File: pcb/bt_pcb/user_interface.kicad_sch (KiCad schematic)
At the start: 69 parts, among them J10 AudioJack3_Switch, J11 AudioJack3_Switch, J16 AudioJack3_Switch, J4 Conn_01x10, J9 AudioJack3_Switch, SW1 SW_Push, SW10 RotaryEncoder_Switch, SW2 SW_Push, SW3 SW_Push, SW4 SW_Push, SW5 SW_Push, SW6 SW_Push, SW7 SW_Push, SW8 SW_Push, SW9 SW_Push

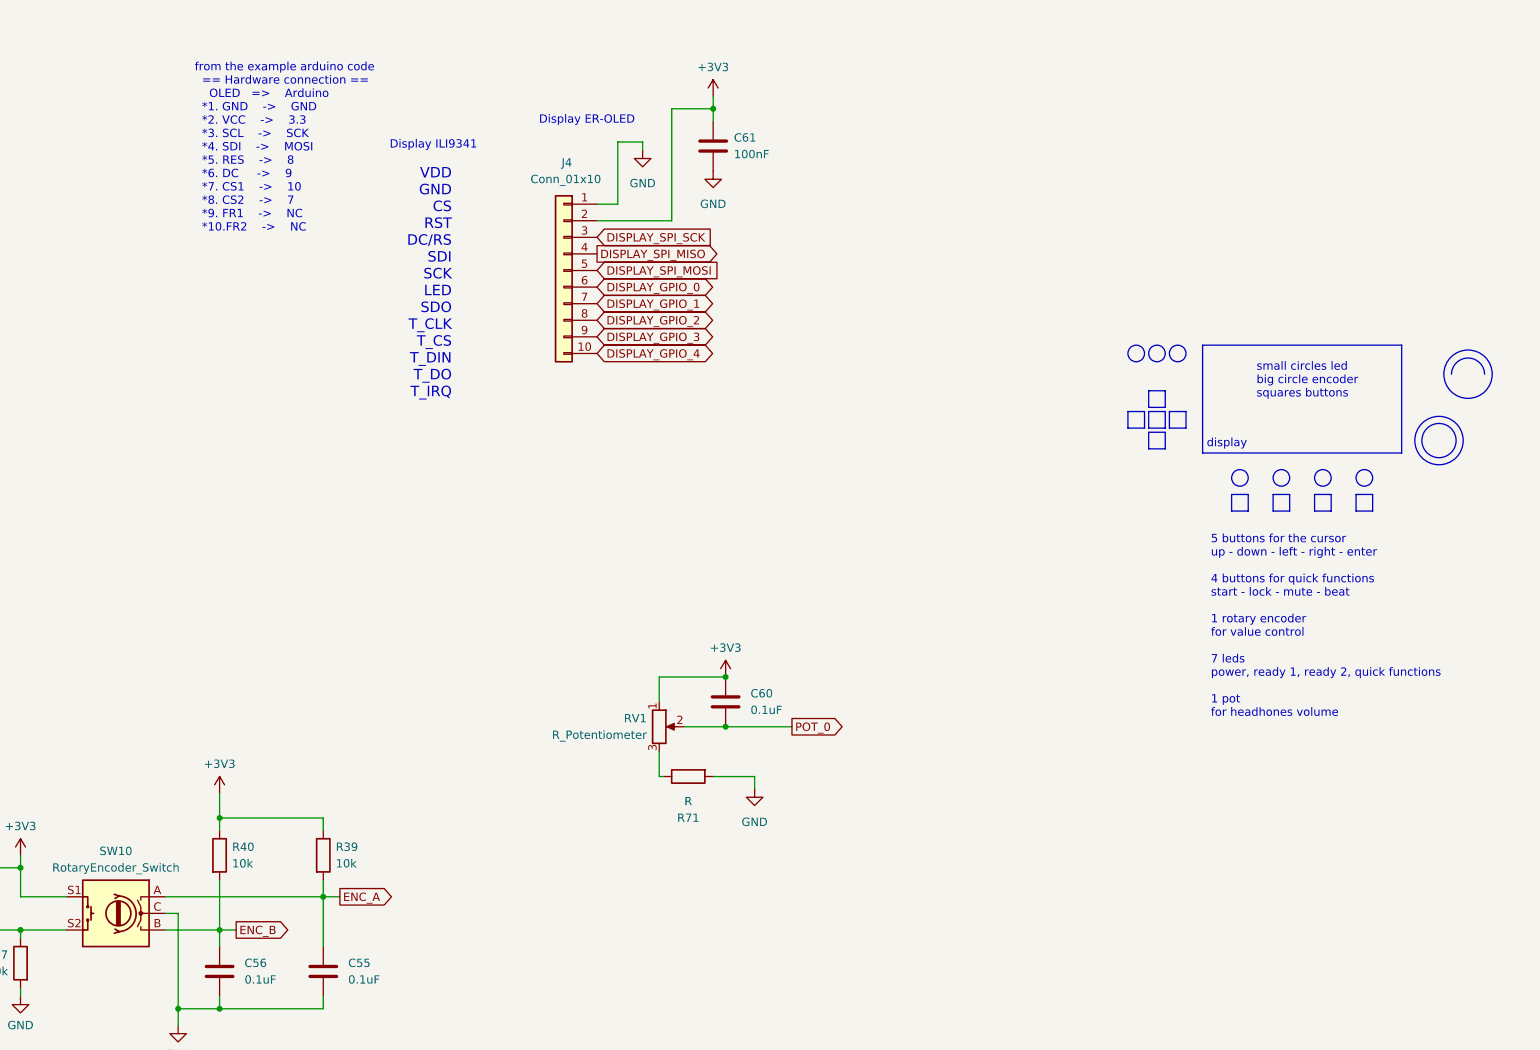
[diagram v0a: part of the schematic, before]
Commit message: ditching power pcb, new codec
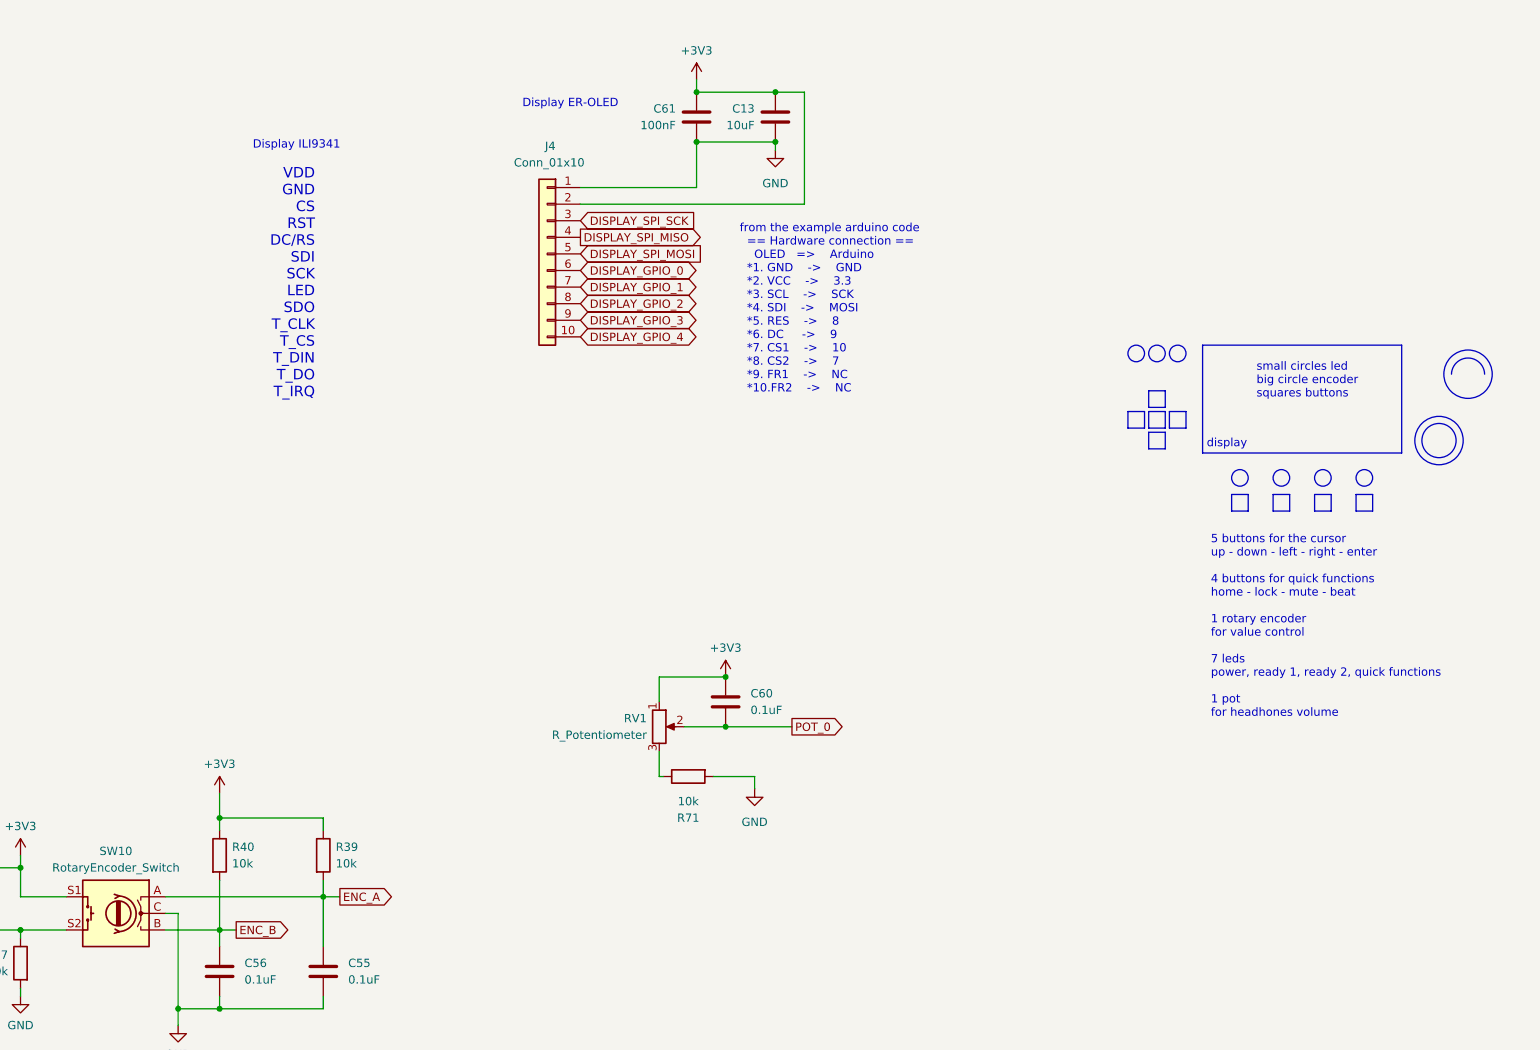
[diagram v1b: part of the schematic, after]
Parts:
- added C13: 10uF, symbol Device:C
- R71: value R -> 10k
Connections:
- net +3V3: now also C13.2
- net GND: now also C13.1
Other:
- note added: "5 buttons for the cursor up - down - left - right - enter 4 buttons for quick functions home - lock - mute - beat 1 rotary encoder for value control 7 leds power, ready 1, ready 2, quick functions 1 pot for headhones volume"
- note removed: "5 buttons for the cursor up - down - left - right - enter 4 buttons for quick functions start - lock - mute - beat 1 rotary encoder for value control 7 leds power, ready 1, ready 2, quick functions 1 pot for headhones volume"
- moved on the sheet: C61, J4

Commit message: big progress, now revising error and warnings
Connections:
- net BTN_0 renamed BTN_0_J
- net BTN_1 renamed BTN_1_J
- net BTN_2 renamed BTN_2_J
- net BTN_3 renamed BTN_3_J
- net BTN_4 renamed BTN_4_J
- net BTN_5 renamed BTN_5_QB
- net BTN_6 renamed BTN_6_QB
- net BTN_7 renamed BTN_7_QB
- net BTN_8 renamed BTN_8_QB
- net LED_0 renamed LED_0_RD
- net LED_1 renamed LED_1_RD
- net LED_2 renamed LED_2_QB
- net LED_3 renamed LED_3_QB
- net LED_4 renamed LED_4_QB
- net LED_5 renamed LED_5_QB
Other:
- note added: "2 leds are "mcu ready" so one for h750 and one for h523"
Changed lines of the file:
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@@
+		)
+	)
+	(text "2 leds are \"mcu ready\"\nso one for h750 and one for h523"
+		(exclude_from_sim no)
+		(at 332.74 138.43 0)
+		(effects
+			(font
+				(size 1.27 1.27)
+			)
 		)
 	)
@@
 	(wire
 		(pts
-			(xy 349.25 190.5) (xy 347.345 190.5)
+			(xy 347.98 190.5) (xy 347.345 190.5)
 		)
 		(stroke
@@
 	(wire
 		(pts
-			(xy 323.85 190.5) (xy 321.945 190.5)
+			(xy 322.58 190.5) (xy 321.945 190.5)
 		)
 		(stroke
@@
 	(wire
 		(pts
-			(xy 298.45 190.5) (xy 296.545 190.5)
+			(xy 297.18 190.5) (xy 296.545 190.5)
 		)
 		(stroke
@@
 	(wire
 		(pts
-			(xy 336.55 190.5) (xy 334.645 190.5)
+			(xy 335.28 190.5) (xy 334.645 190.5)
 		)
 		(stroke
@@
 	(wire
 		(pts
-			(xy 361.95 190.5) (xy 360.045 190.5)
-		)
-		(stroke
-			(width 0)
-			(type default)
-		)
-	)
-	(wire
-		(pts
-			(xy 311.15 190.5) (xy 309.245 190.5)
+			(xy 360.68 190.5) (xy 360.045 190.5)
+		)
+		(stroke
+			(width 0)
+			(type default)
+		)
+	)
+	(wire
+		(pts
+			(xy 309.88 190.5) (xy 309.245 190.5)
 		)
 		(stroke
@@
 	)
 	(global_label "EXP_SW_0"
-		(shape output)
+		(shape passive)
 		(at 62.865 34.29 0)
 		(fields_autoplaced yes)
@@
 		)
 		(property "Intersheetrefs" "${INTERSHEET_REFS}"
-			(at 75.2843 34.29 0)
+			(at 74.173 34.29 0)
 			(effects
 				(font
@@
 		)
 	)
-	(global_label "LED_3"
-		(shape input)
-		(at 336.55 190.5 0)
+	(global_label "LED_3_QB"
+		(shape passive)
+		(at 335.28 190.5 0)
 		(fields_autoplaced yes)
 		(effects
@@
 		)
 		(property "Intersheetrefs" "${INTERSHEET_REFS}"
-			(at 345.1594 190.5 0)
+			(at 346.3462 190.5 0)
 			(effects
 				(font
@@
 	)
 	(global_label "EXP_SW_3"
-		(shape output)
+		(shape passive)
 		(at 62.865 132.08 0)
 		(fields_autoplaced yes)
@@
 		)
 		(property "Intersheetrefs" "${INTERSHEET_REFS}"
-			(at 75.2843 132.08 0)
+			(at 74.173 132.08 0)
 			(effects
 				(font
@@
 		)
 	)
-	(global_label "LED_0"
-		(shape input)
-		(at 298.45 190.5 0)
+	(global_label "LED_0_RD"
+		(shape passive)
+		(at 297.18 190.5 0)
 		(fields_autoplaced yes)
 		(effects
@@
 		)
 		(property "Intersheetrefs" "${INTERSHEET_REFS}"
-			(at 307.0594 190.5 0)
+			(at 308.1857 190.5 0)
 			(effects
 				(font
@@
 		)
 	)
-	(global_label "BTN_1"
-		(shape output)
+	(global_label "BTN_1_J"
+		(shape passive)
 		(at 67.31 226.695 180)
 		(fields_autoplaced yes)
@@
 		)
 		(property "Intersheetrefs" "${INTERSHEET_REFS}"
-			(at 58.5796 226.695 0)
+			(at 57.7557 226.695 0)
 			(effects
 				(font
@@
 	)
 	(global_label "EXP_SW_1"
-		(shape output)
+		(shape passive)
 		(at 62.865 67.31 0)
 		(fields_autoplaced yes)
@@
 		)
 		(property "Intersheetrefs" "${INTERSHEET_REFS}"
-			(at 75.2843 67.31 0)
+			(at 74.173 67.31 0)
 			(effects
 				(font
@@
 		)
 	)
-	(global_label "BTN_0"
-		(shape output)
+	(global_label "BTN_0_J"
+		(shape passive)
 		(at 34.29 226.695 180)
 		(fields_autoplaced yes)
@@
 		)
 		(property "Intersheetrefs" "${INTERSHEET_REFS}"
-			(at 25.5596 226.695 0)
+			(at 24.7357 226.695 0)
 			(effects
 				(font
@@
 		)
 	)
-	(global_label "LED_2"
-		(shape input)
-		(at 323.85 190.5 0)
+	(global_label "LED_2_QB"
+		(shape passive)
+		(at 322.58 190.5 0)
 		(fields_autoplaced yes)
 		(effects
@@
 		)
 		(property "Intersheetrefs" "${INTERSHEET_REFS}"
-			(at 332.4594 190.5 0)
+			(at 333.6462 190.5 0)
 			(effects
 				(font
@@
 		)
 	)
-	(global_label "LED_5"
-		(shape input)
-		(at 361.95 190.5 0)
+	(global_label "LED_5_QB"
+		(shape passive)
+		(at 360.68 190.5 0)
 		(fields_autoplaced yes)
 		(effects
@@
 		)
 		(property "Intersheetrefs" "${INTERSHEET_REFS}"
-			(at 370.5594 190.5 0)
+			(at 371.7462 190.5 0)
 			(effects
 				(font
@@
 	)
 	(global_label "ENC_SW"
-		(shape output)
+		(shape passive)
 		(at 132.715 158.75 180)
 		(fields_autoplaced yes)
@@
 		)
 		(property "Intersheetrefs" "${INTERSHEET_REFS}"
-			(at 122.3518 158.75 0)
+			(at 123.4631 158.75 0)
 			(effects
 				(font
@@
 		)
 	)
-	(global_label "LED_4"
-		(shape input)
-		(at 349.25 190.5 0)
+	(global_label "LED_4_QB"
+		(shape passive)
+		(at 347.98 190.5 0)
 		(fields_autoplaced yes)
 		(effects
@@
 		)
 		(property "Intersheetrefs" "${INTERSHEET_REFS}"
-			(at 357.8594 190.5 0)
+			(at 359.0462 190.5 0)
 			(effects
 				(font
@@
 		)
 	)
-	(global_label "LED_1"
-		(shape input)
-		(at 311.15 190.5 0)
+	(global_label "LED_1_RD"
+		(shape passive)
+		(at 309.88 190.5 0)
 		(fields_autoplaced yes)
 		(effects
@@
 		)
 		(property "Intersheetrefs" "${INTERSHEET_REFS}"
-			(at 319.7594 190.5 0)
+			(at 320.8857 190.5 0)
 			(effects
 				(font
@@
 		)
 	)
-	(global_label "BTN_4"
-		(shape output)
+	(global_label "BTN_4_J"
+		(shape passive)
 		(at 166.37 226.695 180)
 		(fields_autoplaced yes)
@@
 		)
 		(property "Intersheetrefs" "${INTERSHEET_REFS}"
-			(at 157.6396 226.695 0)
+			(at 156.8157 226.695 0)
 			(effects
 				(font
@@
 		)
 	)
-	(global_label "BTN_5"
-		(shape output)
+	(global_label "BTN_5_QB"
+		(shape passive)
 		(at 34.29 260.35 180)
 		(fields_autoplaced yes)
@@
 		)
 		(property "Intersheetrefs" "${INTERSHEET_REFS}"
-			(at 25.5596 260.35 0)
+			(at 23.1028 260.35 0)
 			(effects
 				(font
@@
 		)
 	)
-	(global_label "BTN_3"
-		(shape output)
+	(global_label "BTN_3_J"
+		(shape passive)
 		(at 133.35 226.695 180)
 		(fields_autoplaced yes)
@@
 		)
 		(property "Intersheetrefs" "${INTERSHEET_REFS}"
-			(at 124.6196 226.695 0)
+			(at 123.7957 226.695 0)
 			(effects
 				(font
@@
 		)
 	)
-	(global_label "BTN_7"
-		(shape output)
+	(global_label "BTN_7_QB"
+		(shape passive)
 		(at 100.33 260.35 180)
 		(fields_autoplaced yes)
@@
 		)
 		(property "Intersheetrefs" "${INTERSHEET_REFS}"
-			(at 91.5996 260.35 0)
+			(at 89.1428 260.35 0)
 			(effects
 				(font
@@
 		)
 	)
-	(global_label "BTN_2"
-		(shape output)
+	(global_label "BTN_2_J"
+		(shape passive)
 		(at 100.33 226.695 180)
 		(fields_autoplaced yes)
@@
 		)
 		(property "Intersheetrefs" "${INTERSHEET_REFS}"
-			(at 91.5996 226.695 0)
+			(at 90.7757 226.695 0)
 			(effects
 				(font
@@
 		)
 	)
-	(global_label "BTN_6"
-		(shape output)
+	(global_label "BTN_6_QB"
+		(shape passive)
 		(at 67.31 260.35 180)
 		(fields_autoplaced yes)
@@
 		)
 		(property "Intersheetrefs" "${INTERSHEET_REFS}"
-			(at 58.5796 260.35 0)
+			(at 56.1228 260.35 0)
 			(effects
 				(font
@@
 		)
 	)
-	(global_label "BTN_8"
-		(shape output)
+	(global_label "BTN_8_QB"
+		(shape passive)
 		(at 133.35 260.35 180)
 		(fields_autoplaced yes)
@@
 		)
 		(property "Intersheetrefs" "${INTERSHEET_REFS}"
-			(at 124.6196 260.35 0)
+			(at 122.1628 260.35 0)
 			(effects
 				(font
@@
 	)
 	(global_label "EXP_SW_2"
-		(shape output)
+		(shape passive)
 		(at 62.865 100.33 0)
 		(fields_autoplaced yes)
@@
 		)
 		(property "Intersheetrefs" "${INTERSHEET_REFS}"
-			(at 75.2843 100.33 0)
-			(effects
-				(font
+			(at 74.173 100.33 0)
+			(effects
+				(font

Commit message: solving some erc warnings and errors
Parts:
- removed D10, D2: LED, symbol Device:LED
- added D3, D4: LED, symbol Device:LED
- renumbered C50 to C24, C46 to C25, C52 to C26, C51 to C27, C53 to C28, C116 to C29, C42 to C30, C47 to C31, C43 to C32, C48 to C33, C54 to C34, C44 to C35, C49 to C36, C56 to C37, C45 to C38, C55 to C39, C61 to C40, C60 to C41, C13 to C42, J9 to J5, J10 to J6, J11 to J7, J16 to J8, J4 to J9, R33 to R10, R35 to R11, R78 to R12, R25 to R13, R28 to R14, R32 to R15, R34 to R16, R36 to R17, R79 to R18, R23 to R19, R29 to R20, R24 to R21, R30 to R22, R37 to R23, R26 to R24, R40 to R25, R39 to R26, R71 to R27, R4 to R28, R38 to R29, R41 to R30, R42 to R31, R43 to R32, R68 to R33, R69 to R34, R31 to R7, R27 to R8, R22 to R9, RV1 to RV4, SW9 to SW1, SW4 to SW10, SW5 to SW2, SW1 to SW3, SW6 to SW4, SW2 to SW5, SW7 to SW6, SW3 to SW7, SW10 to SW9
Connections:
- net GND: now also D3.1 (K), D4.1 (K)
- net at R30.2: now also D5.2 (A); no longer D7.2 (A)
- net at R31.2: now also D6.2 (A); no longer D8.2 (A)
- net at R34.2: now also D9.2 (A)
- net at R32.2: now also D7.2 (A); no longer D9.2 (A)
- net at R28.2: now also D3.2 (A)
- net at R33.2: now also D8.2 (A); no longer D5.2 (A)
- net at R29.2: now also D4.2 (A); no longer D6.2 (A)
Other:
- moved on the sheet: C24, C30, C32, C34, C35, C37, C38, C41, C42, J5, J6, J7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

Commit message: schematic in theory finished
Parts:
- removed J5, J6, J7, J8: AudioJack3_Switch, symbol Connector_Audio:AudioJack3_Switch
- added J10, J6, J8, J9: Conn_01x04, Connector_PinHeader_2.54mm:PinHeader_1x04_P2.54mm_Vertical, symbol Connector_Generic:Conn_01x04
- C24: renamed from C26; value 0.1uF -> 100n; footprint (none) -> Capacitor_SMD:C_0603_1608Metric_Pad1.08x0.95mm_HandSolder
- C25: renamed from C40; value 100nF -> 100n; footprint (none) -> Capacitor_SMD:C_0603_1608Metric_Pad1.08x0.95mm_HandSolder
- C26: renamed from C42; value 10uF -> 10u; footprint (none) -> Capacitor_SMD:C_0805_2012Metric_Pad1.18x1.45mm_HandSolder
- C27, C28, C38: value 0.1uF -> 100n; footprint (none) -> Capacitor_SMD:C_0603_1608Metric_Pad1.08x0.95mm_HandSolder
- C29: renamed from C41; value 0.1uF -> 100n; footprint (none) -> Capacitor_SMD:C_0603_1608Metric_Pad1.08x0.95mm_HandSolder
- C30: renamed from C29; value 0.1uF -> 100n; footprint (none) -> Capacitor_SMD:C_0603_1608Metric_Pad1.08x0.95mm_HandSolder
- C31: renamed from C34; value 0.1uF -> 100n; footprint (none) -> Capacitor_SMD:C_0603_1608Metric_Pad1.08x0.95mm_HandSolder
- C32: renamed from C37; value 0.1uF -> 100n; footprint (none) -> Capacitor_SMD:C_0603_1608Metric_Pad1.08x0.95mm_HandSolder
- C33: renamed from C39; value 0.1uF -> 100n; footprint (none) -> Capacitor_SMD:C_0603_1608Metric_Pad1.08x0.95mm_HandSolder
- C34: renamed from C24; value 0.1uF -> 100n; footprint (none) -> Capacitor_SMD:C_0603_1608Metric_Pad1.08x0.95mm_HandSolder
- C35: renamed from C30; value 0.1uF -> 100n; footprint (none) -> Capacitor_SMD:C_0603_1608Metric_Pad1.08x0.95mm_HandSolder
- C36: renamed from C32; value 0.1uF -> 100n; footprint (none) -> Capacitor_SMD:C_0603_1608Metric_Pad1.08x0.95mm_HandSolder
- C37: renamed from C35; value 0.1uF -> 100n; footprint (none) -> Capacitor_SMD:C_0603_1608Metric_Pad1.08x0.95mm_HandSolder
- C39: renamed from C25; value 0.1uF -> 100n; footprint (none) -> Capacitor_SMD:C_0603_1608Metric_Pad1.08x0.95mm_HandSolder
- C40: renamed from C31; value 0.1uF -> 100n; footprint (none) -> Capacitor_SMD:C_0603_1608Metric_Pad1.08x0.95mm_HandSolder
- C41: renamed from C33; value 0.1uF -> 100n; footprint (none) -> Capacitor_SMD:C_0603_1608Metric_Pad1.08x0.95mm_HandSolder
- C42: renamed from C36; value 0.1uF -> 100n; footprint (none) -> Capacitor_SMD:C_0603_1608Metric_Pad1.08x0.95mm_HandSolder
- D3, D4, D5, D6, D7, D8, D9: footprint (none) -> LED_SMD:LED_0603_1608Metric_Pad1.05x0.95mm_HandSolder
- J7: renamed from J9; footprint (none) -> Connector_PinHeader_2.54mm:PinHeader_1x01_P2.54mm_Vertical
- R11: renamed from R15; footprint (none) -> Resistor_SMD:R_0603_1608Metric_Pad0.98x0.95mm_HandSolder
- R12: renamed from R9; footprint (none) -> Resistor_SMD:R_0603_1608Metric_Pad0.98x0.95mm_HandSolder
- R13: renamed from R16; footprint (none) -> Resistor_SMD:R_0603_1608Metric_Pad0.98x0.95mm_HandSolder
- R14: renamed from R10; footprint (none) -> Resistor_SMD:R_0603_1608Metric_Pad0.98x0.95mm_HandSolder
- R15: renamed from R17; footprint (none) -> Resistor_SMD:R_0603_1608Metric_Pad0.98x0.95mm_HandSolder
- R16: renamed from R11; footprint (none) -> Resistor_SMD:R_0603_1608Metric_Pad0.98x0.95mm_HandSolder
- R17: renamed from R18; footprint (none) -> Resistor_SMD:R_0603_1608Metric_Pad0.98x0.95mm_HandSolder
- R18: renamed from R27; footprint (none) -> Resistor_SMD:R_0603_1608Metric_Pad0.98x0.95mm_HandSolder
- R19: renamed from R12; footprint (none) -> Resistor_SMD:R_0603_1608Metric_Pad0.98x0.95mm_HandSolder
- R20: renamed from R25; footprint (none) -> Resistor_SMD:R_0603_1608Metric_Pad0.98x0.95mm_HandSolder
- R21: renamed from R26; footprint (none) -> Resistor_SMD:R_0603_1608Metric_Pad0.98x0.95mm_HandSolder
- R22: renamed from R23; footprint (none) -> Resistor_SMD:R_0603_1608Metric_Pad0.98x0.95mm_HandSolder
- R23: renamed from R28; footprint (none) -> Resistor_SMD:R_0603_1608Metric_Pad0.98x0.95mm_HandSolder
- R24: renamed from R29; footprint (none) -> Resistor_SMD:R_0603_1608Metric_Pad0.98x0.95mm_HandSolder
- R25: renamed from R30; footprint (none) -> Resistor_SMD:R_0603_1608Metric_Pad0.98x0.95mm_HandSolder
- R26: renamed from R31; footprint (none) -> Resistor_SMD:R_0603_1608Metric_Pad0.98x0.95mm_HandSolder
- R27: renamed from R32; footprint (none) -> Resistor_SMD:R_0603_1608Metric_Pad0.98x0.95mm_HandSolder
- R28: renamed from R33; footprint (none) -> Resistor_SMD:R_0603_1608Metric_Pad0.98x0.95mm_HandSolder
- R29: renamed from R34; footprint (none) -> Resistor_SMD:R_0603_1608Metric_Pad0.98x0.95mm_HandSolder
- R30: renamed from R7; footprint (none) -> Resistor_SMD:R_0603_1608Metric_Pad0.98x0.95mm_HandSolder
- R31: renamed from R13; footprint (none) -> Resistor_SMD:R_0603_1608Metric_Pad0.98x0.95mm_HandSolder
- R32: renamed from R19; footprint (none) -> Resistor_SMD:R_0603_1608Metric_Pad0.98x0.95mm_HandSolder
- R33: renamed from R21; footprint (none) -> Resistor_SMD:R_0603_1608Metric_Pad0.98x0.95mm_HandSolder
- R34: renamed from R24; footprint (none) -> Resistor_SMD:R_0603_1608Metric_Pad0.98x0.95mm_HandSolder
- R35: renamed from R8; footprint (none) -> Resistor_SMD:R_0603_1608Metric_Pad0.98x0.95mm_HandSolder
- R36: renamed from R14; footprint (none) -> Resistor_SMD:R_0603_1608Metric_Pad0.98x0.95mm_HandSolder
- R37: renamed from R20; footprint (none) -> Resistor_SMD:R_0603_1608Metric_Pad0.98x0.95mm_HandSolder
- R38: renamed from R22; footprint (none) -> Resistor_SMD:R_0603_1608Metric_Pad0.98x0.95mm_HandSolder
- RV4: footprint (none) -> Connector_PinHeader_2.54mm:PinHeader_1x03_P2.54mm_Vertical
- SW1: renamed from SW9; footprint (none) -> Connector_PinHeader_2.54mm:PinHeader_1x05_P2.54mm_Vertical
- SW10: renamed from SW8; footprint (none) -> Button_Switch_THT:SW_TH_Tactile_Omron_B3F-102x
- SW2: renamed from SW1; footprint (none) -> Button_Switch_THT:SW_TH_Tactile_Omron_B3F-102x
- SW3: footprint (none) -> Button_Switch_THT:SW_TH_Tactile_Omron_B3F-102x
- SW4: renamed from SW5; footprint (none) -> Button_Switch_THT:SW_TH_Tactile_Omron_B3F-102x
- SW5: renamed from SW7; footprint (none) -> Button_Switch_THT:SW_TH_Tactile_Omron_B3F-102x
- SW6: renamed from SW10; footprint (none) -> Button_Switch_THT:SW_TH_Tactile_Omron_B3F-102x
- SW7: renamed from SW2; footprint (none) -> Button_Switch_THT:SW_TH_Tactile_Omron_B3F-102x
- SW8: renamed from SW4; footprint (none) -> Button_Switch_THT:SW_TH_Tactile_Omron_B3F-102x
- SW9: renamed from SW6; footprint (none) -> Button_Switch_THT:SW_TH_Tactile_Omron_B3F-102x
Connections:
- net +3V3: now also J10.4 (Pin_4), J6.4 (Pin_4), J8.4 (Pin_4), J9.4 (Pin_4)
- net EXP_0: now also J6.3 (Pin_3)
- net EXP_1: now also J8.3 (Pin_3)
- net EXP_2: now also J9.3 (Pin_3)
- net EXP_3: now also J10.3 (Pin_3)
- net EXP_SW_0: now also J6.2 (Pin_2)
- net EXP_SW_1: now also J8.2 (Pin_2)
- net EXP_SW_2: now also J9.2 (Pin_2)
- net EXP_SW_3: now also J10.2 (Pin_2)
- net GND: now also J10.1 (Pin_1), J6.1 (Pin_1), J8.1 (Pin_1), J9.1 (Pin_1)
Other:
- note added: "T --> 4 R --> 3 SN --> 2 TN, RN, S --> 1"
- note added: "┌┬──────────┐ ▒││▒▒▓▒▓▒ │ └┤ ◊ ◊ ◊ ┌─┼─ TN │ │ │ └────┼── T │ │ │ ┌─┼─ RN │ │ └──────┼── R │ │ ┌─┼─ SN │ └────────┼── S └──────────┘"
- moved on the sheet: C35, C36, C37, C38, C40, C41, C42, R31, R32, R33, R34, R36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

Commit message: pcb started
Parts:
- removed SW1: RotaryEncoder_Switch, Connector_PinHeader_2.54mm:PinHeader_1x05_P2.54mm_Vertical, symbol Device:RotaryEncoder_Switch
- added D10, D12, D14, D16, D4, D6, D8: LED, LED_THT:LED_D3.0mm, symbol Device:LED
- added J12: Conn_01x05, Connector_PinHeader_2.54mm:PinHeader_1x05_P2.54mm_Vertical, symbol Connector_Generic:Conn_01x05
- J8: renamed from J7; footprint Connector_PinHeader_2.54mm:PinHeader_1x01_P2.54mm_Vertical -> Connector_PinHeader_2.54mm:PinHeader_1x10_P2.54mm_Vertical
- renumbered D7 to D11, D8 to D13, D9 to D15, D4 to D5, D5 to D7, D6 to D9, J9 to J10, J10 to J11, J6 to J7, J8 to J9, R11 to R12, R12 to R13, R13 to R14, R14 to R15, R15 to R16, R16 to R17, R17 to R18, R18 to R19, R19 to R20, R20 to R21, R21 to R22, R22 to R23, R23 to R24, R24 to R25, R25 to R26, R26 to R27, R27 to R28, R28 to R29, R29 to R30, R30 to R31, R31 to R32, R32 to R33, R33 to R34, R34 to R35, R35 to R36, R36 to R37, R37 to R38, R38 to R39, SW2 to SW1, SW3 to SW2, SW4 to SW3, SW5 to SW4, SW6 to SW5, SW7 to SW6, SW8 to SW7, SW9 to SW8, SW10 to SW9
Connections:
- net +3V3: now also J12.1 (Pin_1)
- net ENC_A: now also J12.5 (Pin_5)
- net ENC_B: now also J12.3 (Pin_3)
- net ENC_SW: now also J12.2 (Pin_2)
- net GND: now also D10.1 (K), D12.1 (K), D14.1 (K), D16.1 (K), D4.1 (K), D6.1 (K), D8.1 (K), J12.4 (Pin_4)
- net at D7.2 (A), R26.2: now also D8.2 (A)
- net at D3.2 (A), R24.2: now also D4.2 (A)
- net at D9.2 (A), R27.2: now also D10.2 (A)
- net at D15.2 (A), R30.2: now also D16.2 (A)
- net at D13.2 (A), R29.2: now also D14.2 (A)
- net at D11.2 (A), R28.2: now also D12.2 (A)
- net at D5.2 (A), R25.2: now also D6.2 (A)
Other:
- note added: "┌─────────────┐ │ \ ─┼─ A 5 1 S1 ─┼──┐ ▒▒▒ \ │ │ ├ ▒▒▓▒▒ ├─┼─ C 4 2 S2 ─┼──┘ ▒▒▒ / │ │ / ─┼─ B 3 └─────────────┘"
- moved on the sheet: C32, C33, D11, D13, D15, D3, D5, D7, D9, R24, R25, R26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
